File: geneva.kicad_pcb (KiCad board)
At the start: 2 copper layers, 120.3 x 90.8 mm, 22 parts, among them J1 USB_B_Micro

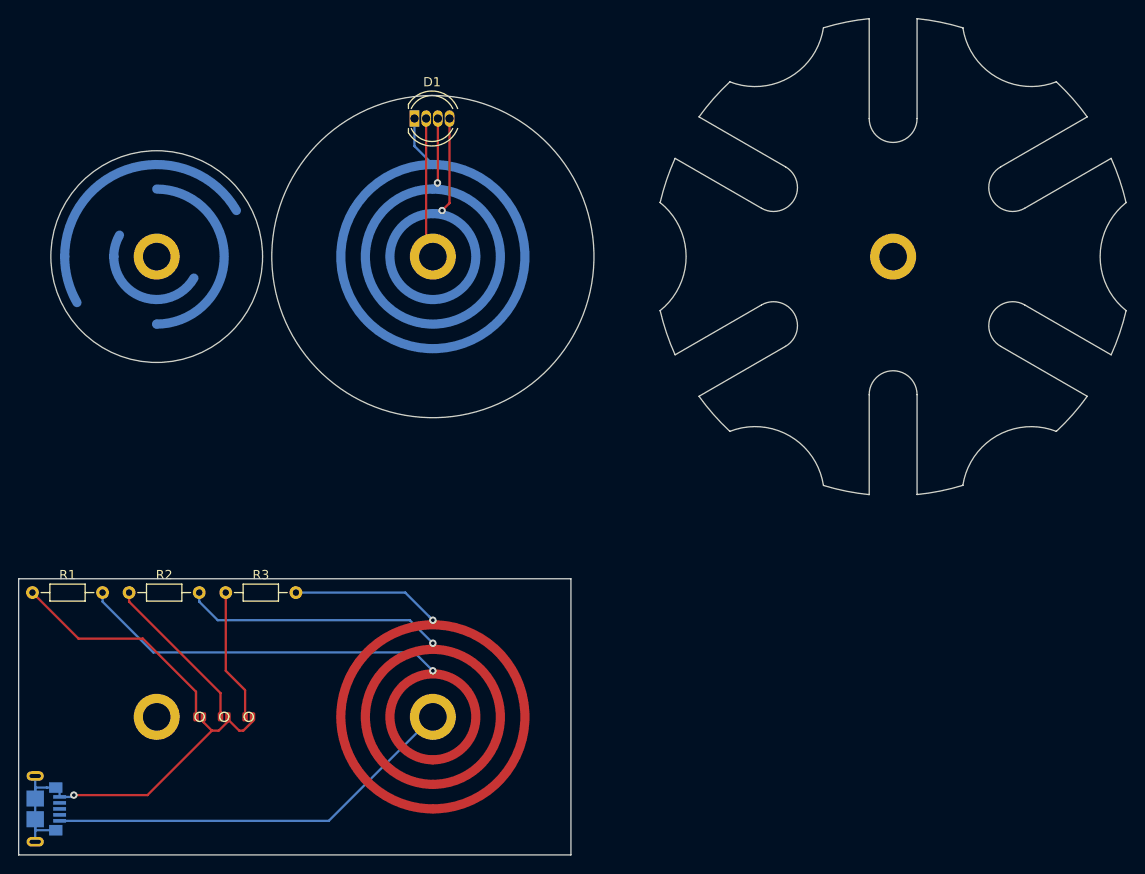
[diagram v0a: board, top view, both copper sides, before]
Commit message: Removed soldermask layer from critical parts of RGB version
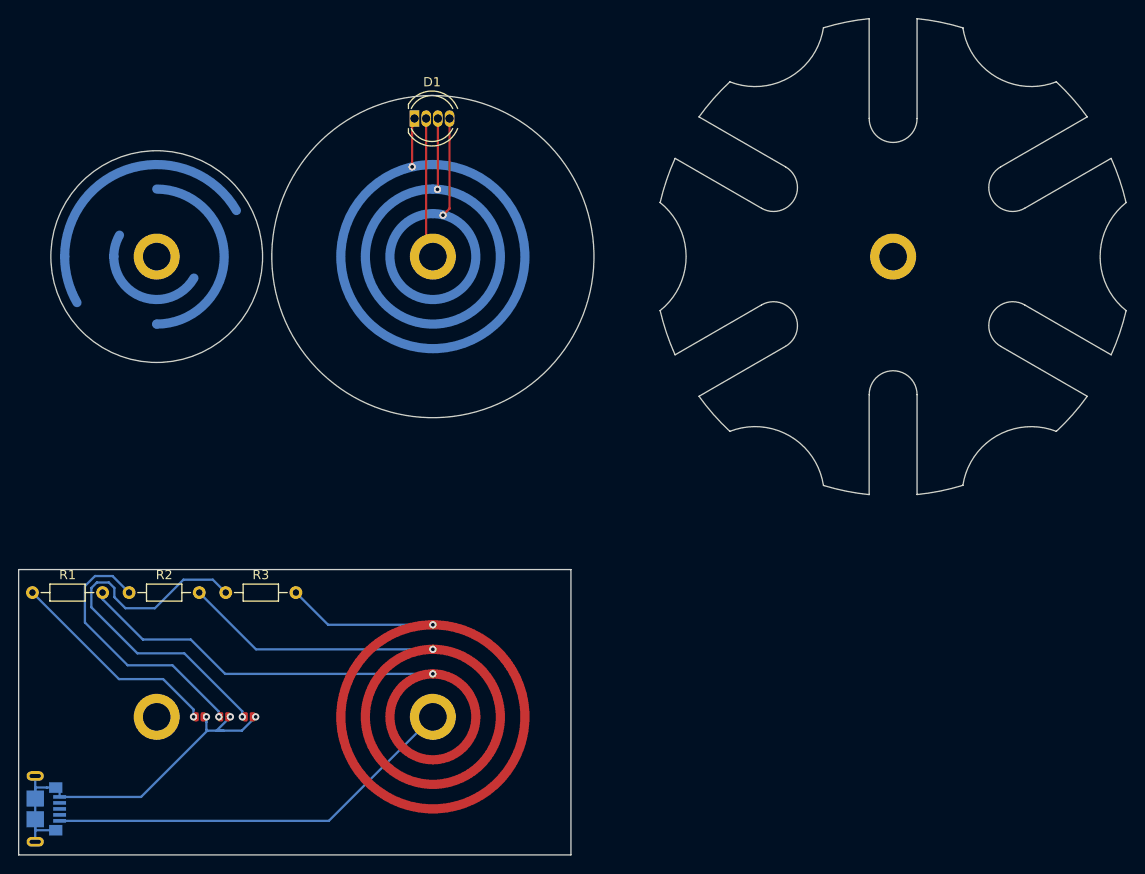
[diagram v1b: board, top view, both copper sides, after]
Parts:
- turned REF** to 180 degrees (x3)
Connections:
- D1 pad 1: redrail -> redwheel
- D1 pad 2: 5V -> 5Vwheel
- D1 pad 3: greenrail -> greenwheel
- D1 pad 4: bluerail -> bluewheel
- REF** pad 1: 5V -> 5Vwheel
- REF** pad 1: redrail -> redwheel
- REF** pad 1: greenrail -> greenwheel
- REF** pad 1: bluerail -> bluewheel
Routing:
- net Net-(JP3-Pad1): track 14.4 -> 42.5 mm, vias 0 -> 1
- net 5Vwheel: track 0.00 -> 15.3 mm
- net 5V: track 60.5 -> 45.2 mm
- net bluewheel: track 0.00 -> 12.0 mm, vias 0 -> 1
- net Net-(JP2-Pad1): track 17.6 -> 29.3 mm, vias 0 -> 1
- net bluerail: track 51.5 -> 40.0 mm, vias 2 -> 1
- net redwheel: track 0.00 -> 9.46 mm, vias 0 -> 1
- net greenwheel: track 0.00 -> 8.23 mm, vias 0 -> 1
- net greenrail: track 36.1 -> 27.9 mm, vias 2 -> 1
- net redrail: track 22.0 -> 16.3 mm
- net 0V: track 43.5 -> 44.8 mm, vias 1 -> 3
- net Net-(JP1-Pad1): track 25.0 -> 23.8 mm, vias 0 -> 1
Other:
- outline, holes or cut-outs redrawn
